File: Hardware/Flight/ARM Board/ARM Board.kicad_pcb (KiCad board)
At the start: 2 copper layers, 82 x 82 mm, 85 parts, among them J1 Conn_01x20_Female, J2 USB_B_Micro, J3 Harwin_M80-5400642, J4 SD_Card, J5 SD_Card, J6 Conn_01x10, Q1 Q_PMOS_GSD, U1 MCP2562-canhw, U2 FT231XS, U3 STM32L4x6RxT6-symbols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

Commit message: ARM board for review
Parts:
- D2, D3, D5, Q1: footprint TO_SOT_Packages_SMD:SOT-23 -> TO_SOT_Packages_SMD:SOT-23_Handsoldering
- VR1: footprint Housings_DFN_QFN:DFN-6-1EP_3x3mm_Pitch0.95mm -> Payload_StandardPackages:DFN-6-1EP_3x3mm_Pitch0.95mm
- moved L1 1.12 mm to (27.7, 37.1)
- moved D3 1.00 mm to (62.1, 25.7)
- moved D2 0.75 mm to (69.6, 25.7)
- moved Q1 0.52 mm to (62.0, 11.1)
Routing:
- net +5V: track 59.3 -> 64.4 mm
- net /5_BUS: track 50.0 -> 54.6 mm
- net Net-(C9-Pad1): track 11.3 -> 14.7 mm
- net /3V3_BUS: track 12.6 -> 15.0 mm
- net +3V3: track 310.3 -> 312.5 mm
- net Net-(JP19-Pad2): track 18.3 -> 20.0 mm
- net /5_USB: track 75.9 -> 77.3 mm
- net /5_CANHW: track 54.7 -> 56.0 mm
- net Net-(D7-Pad1): track 17.4 -> 18.5 mm
- net Net-(C14-Pad1): track 31.7 -> 31.0 mm
- net Net-(D8-Pad1): track 12.9 -> 13.5 mm
- net /ARM&RAMMER/UART_~RTS: track 53.0 -> 52.5 mm

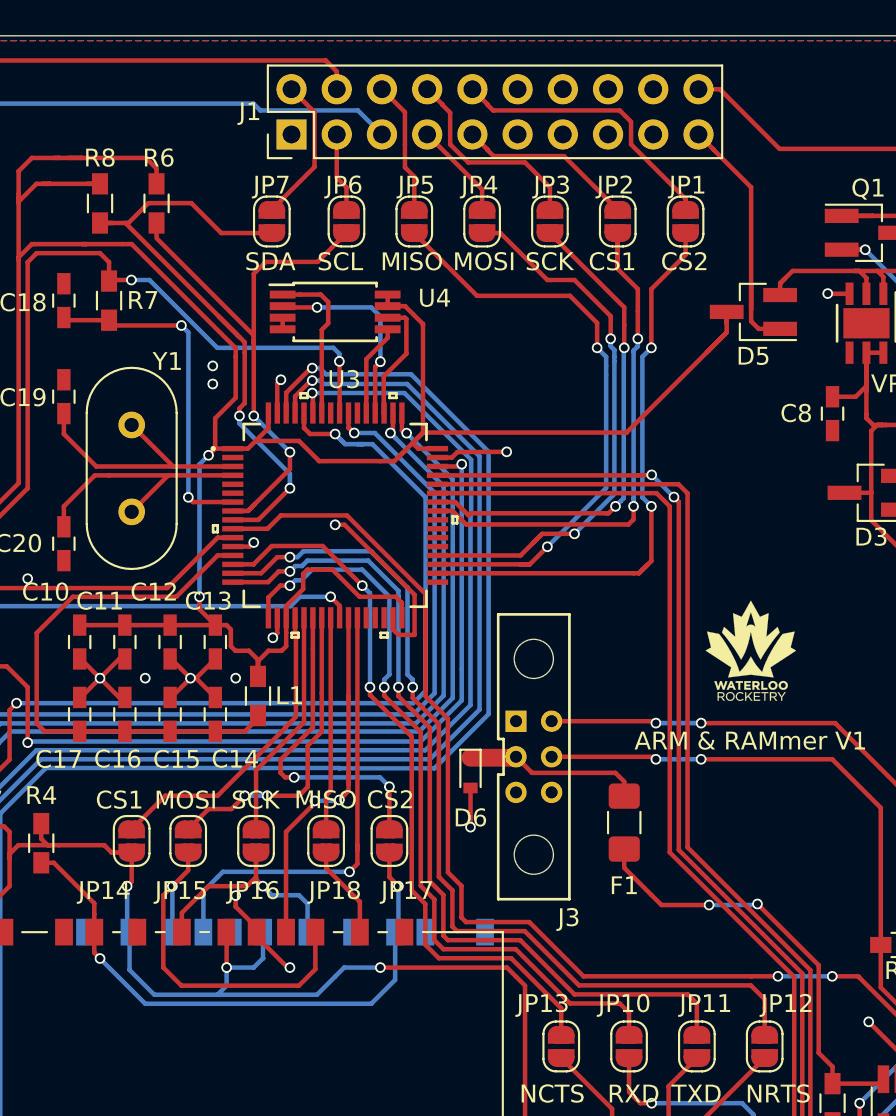
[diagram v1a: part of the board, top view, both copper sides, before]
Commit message: connected GPIO to ARM board
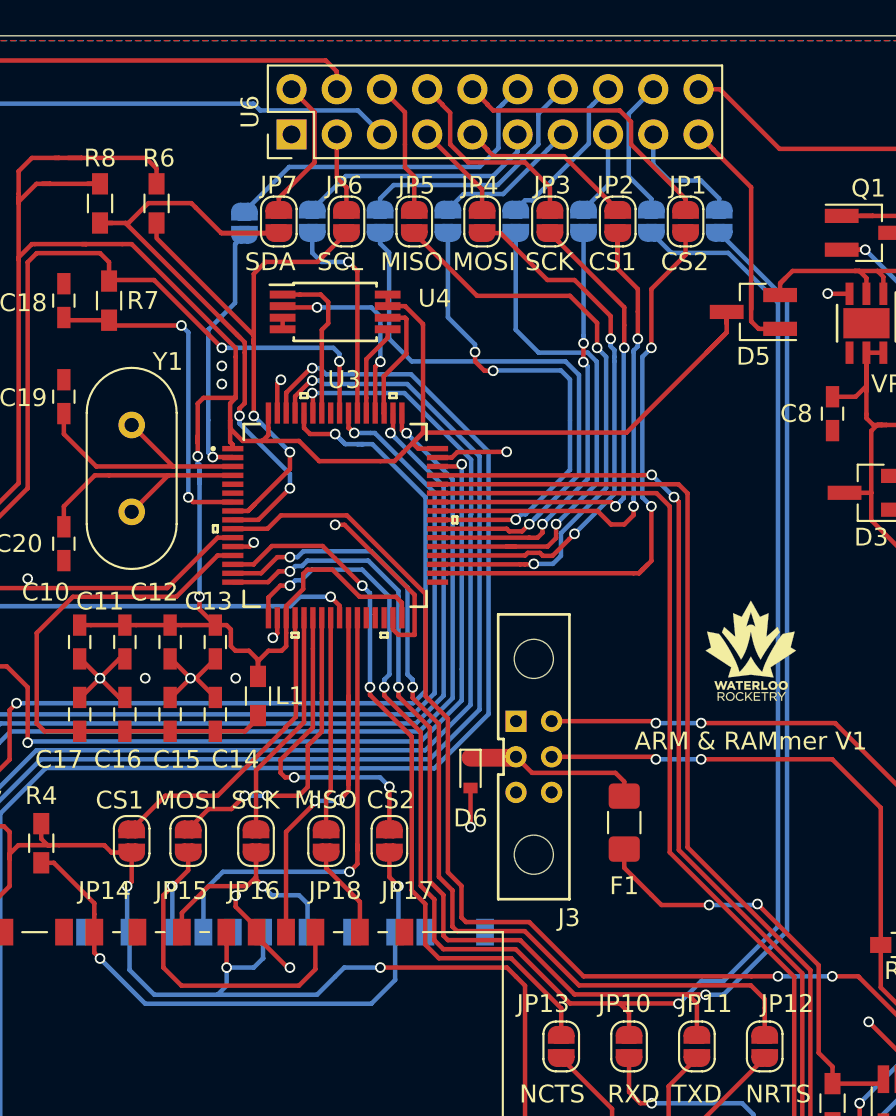
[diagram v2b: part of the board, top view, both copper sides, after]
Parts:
- removed J1: Conn_01x20_Female, Pin_Headers:Pin_Header_Straight_2x10_Pitch2.54mm
- added JP23: Jumper, Jumper:SolderJumper-2_P1.3mm_Open_RoundedPad1.0x1.5mm, B.Cu at (49.8, 10.4)
- added JP24: Jumper, Jumper:SolderJumper-2_P1.3mm_Open_RoundedPad1.0x1.5mm, B.Cu at (53.6, 10.4)
- added JP25: Jumper, Jumper:SolderJumper-2_P1.3mm_Open_RoundedPad1.0x1.5mm, B.Cu at (42.2, 10.4)
- added JP26: Jumper, Jumper:SolderJumper-2_P1.3mm_Open_RoundedPad1.0x1.5mm, B.Cu at (46.0, 10.4)
- added JP27: Jumper, Jumper:SolderJumper-2_P1.3mm_Open_RoundedPad1.0x1.5mm, B.Cu at (34.5, 10.4)
- added JP28: Jumper, Jumper:SolderJumper-2_P1.3mm_Open_RoundedPad1.0x1.5mm, B.Cu at (38.4, 10.4)
- added JP29: Jumper, Jumper:SolderJumper-2_P1.3mm_Open_RoundedPad1.0x1.5mm, B.Cu at (26.9, 10.5)
- added JP30: Jumper, Jumper:SolderJumper-2_P1.3mm_Open_RoundedPad1.0x1.5mm, B.Cu at (30.7, 10.4)
- added U6: Bus_Connector, Payload_Connectors:Pin_Header_Straight_2x10_Pitch2.54mm, F.Cu at (29.6, 5.54)
- moved JP7 0.39 mm to (28.9, 10.4)
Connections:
- U3 pad 2: Net-(U3-Pad2) -> /ARM&RAMMER/RES4
- U3 pad 37: Net-(U3-Pad37) -> /ARM&RAMMER/RES0
- U3 pad 38: Net-(U3-Pad38) -> /ARM&RAMMER/RES1
- U3 pad 39: Net-(U3-Pad39) -> /ARM&RAMMER/RES2
- U3 pad 40: Net-(U3-Pad40) -> /ARM&RAMMER/RES3
- U3 pad 54: Net-(U3-Pad54) -> /ARM&RAMMER/RES5
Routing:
- net /ARM&RAMMER/UART_RX: track 43.7 -> 98.1 mm, vias 2 -> 3
- net /ARM&RAMMER/UART_TX: track 48.5 -> 96.4 mm, vias 2 -> 3
- net /ARM&RAMMER/RES2: track 0.00 -> 33.3 mm, vias 0 -> 1
- net /ARM&RAMMER/RES0: track 0.00 -> 28.9 mm, vias 0 -> 1
- net /ARM&RAMMER/RES3: track 0.00 -> 27.3 mm, vias 0 -> 3
- net /ARM&RAMMER/RES1: track 0.00 -> 24.0 mm, vias 0 -> 3
- net Net-(JP29-Pad1): track 0.00 -> 19.5 mm
- net /ARM&RAMMER/RES4: track 0.00 -> 14.6 mm, vias 0 -> 1
- net Net-(JP27-Pad1): track 0.00 -> 14.4 mm
- net Net-(JP30-Pad1): track 0.00 -> 13.8 mm
- net /ARM&RAMMER/RES5: track 0.00 -> 12.1 mm, vias 0 -> 1
- net Net-(JP25-Pad1): track 0.00 -> 9.14 mm
- net Net-(JP28-Pad1): track 0.00 -> 8.21 mm
- net Net-(JP23-Pad1): track 0.00 -> 7.86 mm
- net Net-(JP24-Pad1): track 0.00 -> 6.80 mm
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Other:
- net class Default: clearance 0.1 -> 0.06
- net class Power: clearance 0.1 -> 0.06
- rule trace_clearance: 0.1 -> 0.06
- board text added: "RS0"
- board text added: "RS1"
- board text added: "RS2"
- board text added: "RS3"
- board text added: "RS4"
- board text added: "RS5"
- board text added: "RX"
- board text added: "TX"

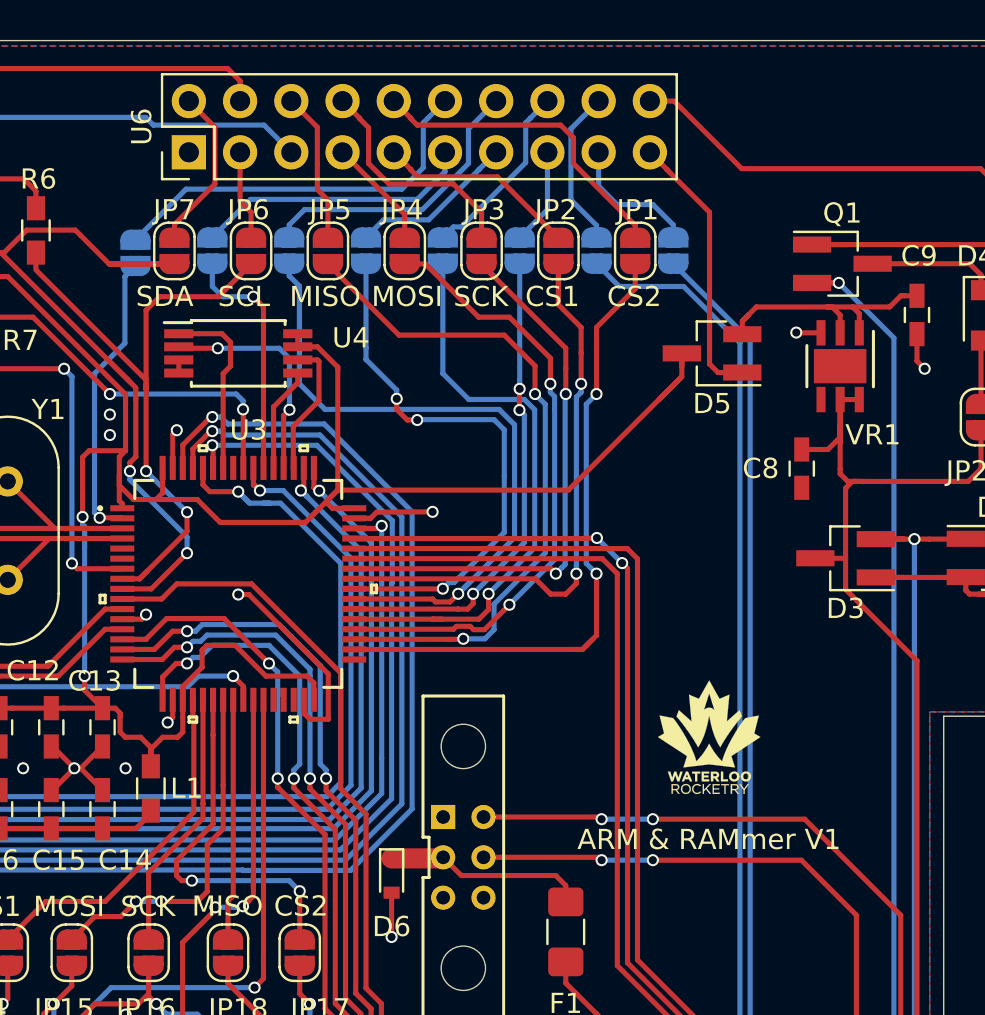
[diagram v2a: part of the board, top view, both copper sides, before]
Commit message: updated battery, experiment board. Added temp sensor to ARM board
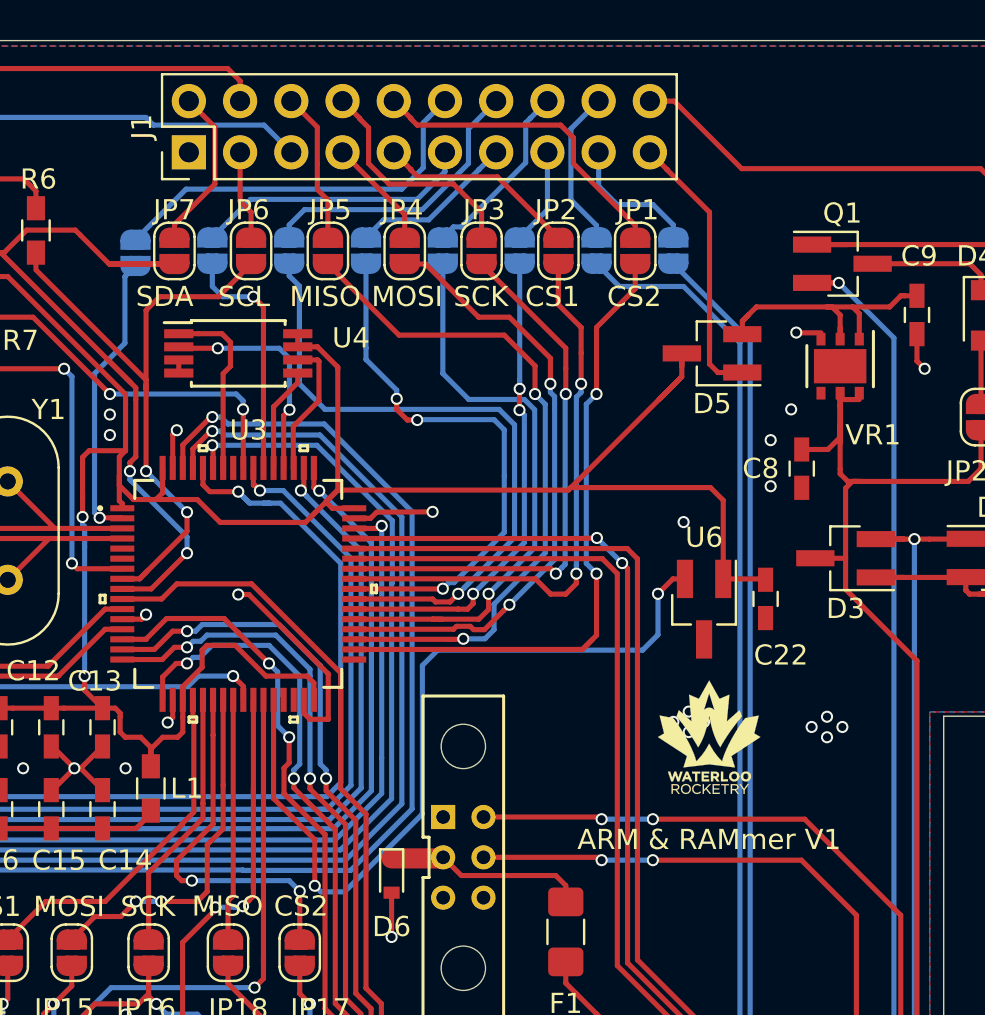
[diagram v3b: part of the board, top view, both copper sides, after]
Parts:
- added C22: 0.1uF, Capacitors_SMD:C_0603_HandSoldering, F.Cu at (58.2, 27.7)
- added J1: Bus_Connector, Payload_Connectors:Pin_Header_Straight_2x10_Pitch2.54mm, F.Cu at (29.6, 5.54)
- U6: value Bus_Connector -> MCP9700AT-ETT; footprint Payload_Connectors:Pin_Header_Straight_2x10_Pitch2.54mm -> TO_SOT_Packages_SMD:SOT-23_Handsoldering
- VR1: footprint Payload_StandardPackages:DFN-6-1EP_3x3mm_Pitch0.95mm -> Housings_DFN_QFN:DFN-6-1EP_3x3mm_Pitch0.95mm
- moved U6 34.1 mm to (55.1, 28.2), turned to 270 degrees
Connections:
- JP1 pad 1: Net-(JP1-Pad1) -> Net-(J1-Pad10)
- JP2 pad 1: Net-(JP2-Pad1) -> Net-(J1-Pad9)
- JP21 pad 1: Net-(JP21-Pad1) -> Net-(J1-Pad5)
- JP22 pad 1: Net-(JP22-Pad1) -> Net-(J1-Pad4)
- JP23 pad 1: Net-(JP23-Pad1) -> Net-(J1-Pad18)
- JP24 pad 1: Net-(JP24-Pad1) -> Net-(J1-Pad17)
- JP25 pad 1: Net-(JP25-Pad1) -> Net-(J1-Pad16)
- JP26 pad 1: Net-(JP26-Pad1) -> Net-(J1-Pad15)
- JP27 pad 1: Net-(JP27-Pad1) -> Net-(J1-Pad14)
- JP28 pad 1: Net-(JP28-Pad1) -> Net-(J1-Pad13)
- JP29 pad 1: Net-(JP29-Pad1) -> Net-(J1-Pad12)
- JP3 pad 1: Net-(JP3-Pad1) -> Net-(J1-Pad8)
- JP30 pad 1: Net-(JP30-Pad1) -> Net-(J1-Pad11)
- JP4 pad 1: Net-(JP4-Pad1) -> Net-(J1-Pad7)
- JP5 pad 1: Net-(JP5-Pad1) -> Net-(J1-Pad6)
- JP6 pad 1: Net-(JP6-Pad1) -> Net-(J1-Pad3)
- JP7 pad 1: Net-(JP7-Pad1) -> Net-(J1-Pad2)
- U3 pad 28: Net-(U3-Pad28) -> /ARM&RAMMER/TEMP
- U6 pad 1: GND -> +3V3
- U6 pad 2: Net-(JP7-Pad1) -> /ARM&RAMMER/TEMP
- U6 pad 3: Net-(JP6-Pad1) -> GND
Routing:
- net Net-(JP22-Pad1): track 45.9 -> 0.00 mm
- net Net-(J1-Pad4): track 0.00 -> 45.9 mm
- net Net-(JP21-Pad1): track 44.6 -> 0.00 mm, vias 1 -> 0
- net Net-(J1-Pad5): track 0.00 -> 44.6 mm, vias 0 -> 1
- net /ARM&RAMMER/TEMP: track 0.00 -> 40.5 mm, vias 0 -> 2
- net Net-(JP29-Pad1): track 19.5 -> 0.00 mm
- net Net-(J1-Pad12): track 0.00 -> 19.5 mm
- net Net-(JP1-Pad1): track 16.1 -> 0.00 mm
- net Net-(J1-Pad10): track 0.00 -> 16.1 mm
- net Net-(JP27-Pad1): track 14.4 -> 0.00 mm
- net Net-(J1-Pad14): track 0.00 -> 14.4 mm
- net Net-(JP30-Pad1): track 13.8 -> 0.00 mm
- net Net-(J1-Pad11): track 0.00 -> 13.8 mm
- net +3V3: track 317.8 -> 331.7 mm
- net Net-(JP3-Pad1): track 11.5 -> 0.00 mm
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
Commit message: addressed Alex's ARM review comments
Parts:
- removed R7: 0, Resistors_SMD:R_0603_HandSoldering
- added JP31: Jumper, Jumper:SolderJumper-2_P1.3mm_Open_RoundedPad1.0x1.5mm, F.Cu at (19.6, 15.0)
- C17: value 100uF -> 100nF
- VR1: footprint Housings_DFN_QFN:DFN-6-1EP_3x3mm_Pitch0.95mm -> Payload_StandardPackages:DFN-6-1EP_3x3mm_Pitch0.95mm
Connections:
- net /ARM&RAMMER/RES4 renamed /ARM&RAMMER/~FAULT1
- net /ARM&RAMMER/RES5 renamed /ARM&RAMMER/~FAULT2
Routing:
- net /ARM&RAMMER/~(JTRST|RST): track 61.5 -> 64.1 mm
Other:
- outline, holes or cut-outs redrawn
- board text added: "1"
- board text added: "10"
- board text added: "~JRST"
